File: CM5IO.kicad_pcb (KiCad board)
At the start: 4 copper layers, 65 parts, among them J10 690-019-298-412, J11 USB_C_Receptacle_USB2.0, J12 USB3_A, J14 JST_SHBM04B-SRSS-TB, J16 Conn_01x22_Female, J2 Conn_02x07_Odd_Even, J22 690-019-298-412, J3 Conn_01x03, J4 Bus_M.2_Socket_M, J5 Conn_01x22_Female, J6 THD-02-R, J8 THD-20-R, SW1 Right angle Tact button, U12 RT9742SNGV, U5 74LVC1G07SE-7, U6 AP22653W6, U7 ASEK-32.768KHZ-L-R-T, U8 AP3441SHE-7B

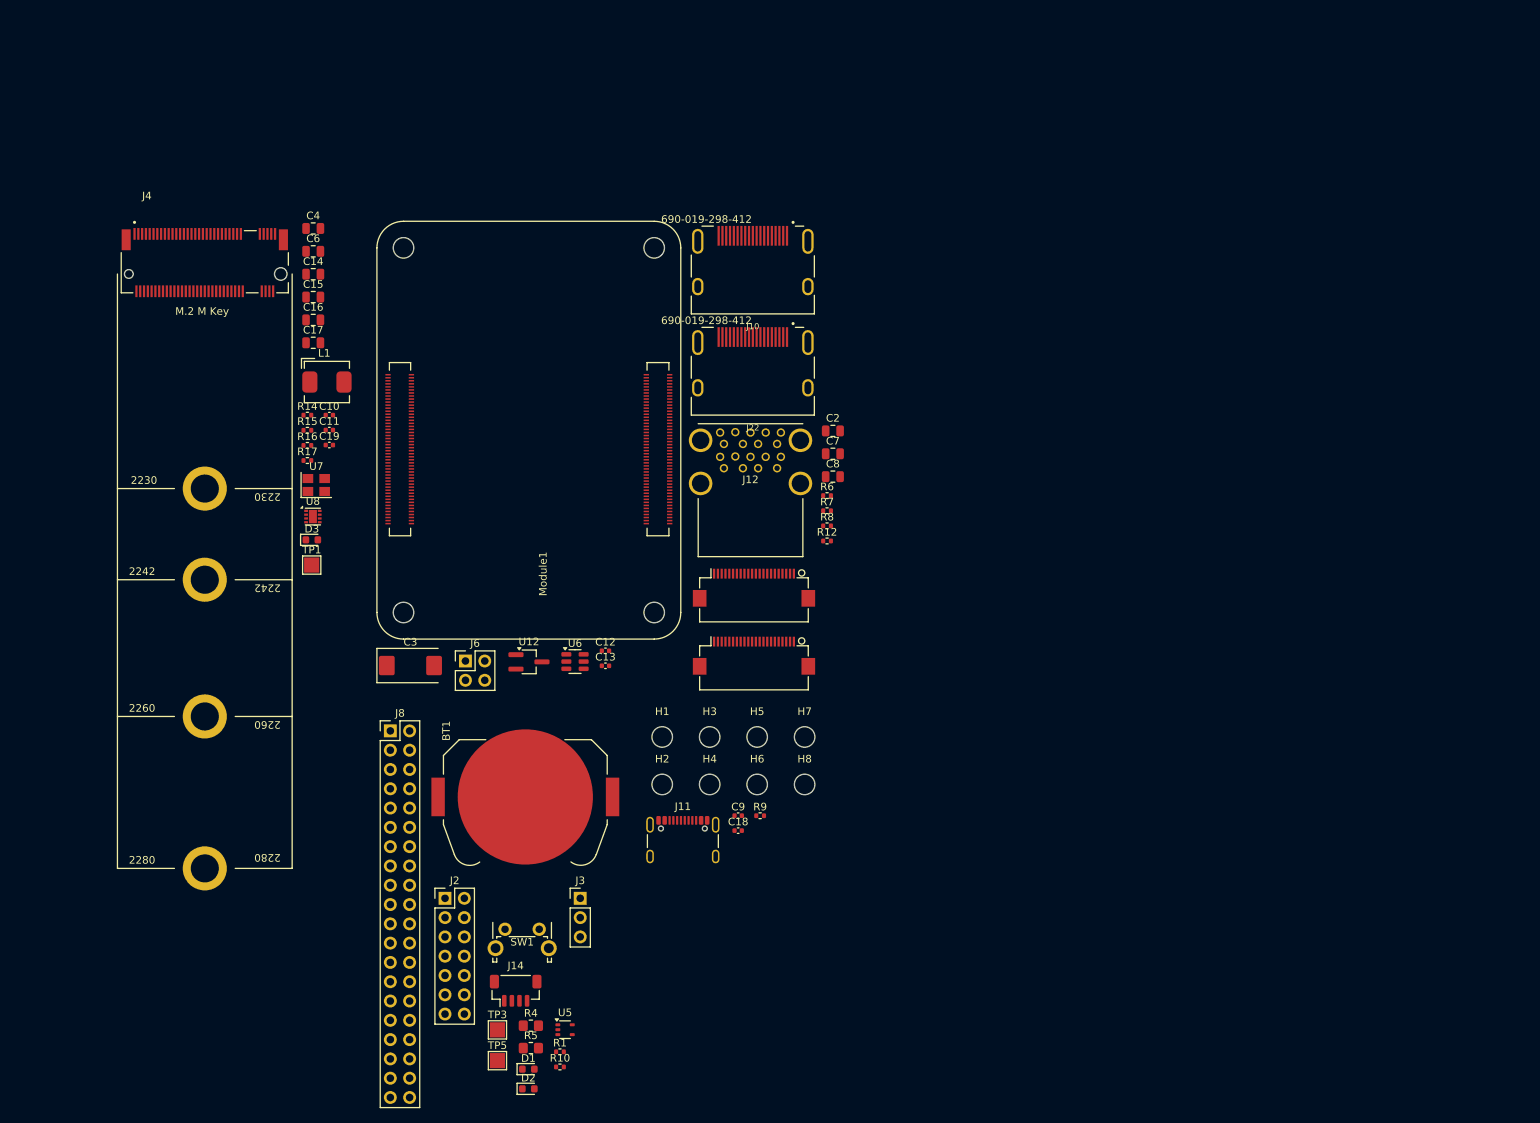
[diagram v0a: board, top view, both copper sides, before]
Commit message: Removing unwanted sections, such that the carrier board is a blank canvas
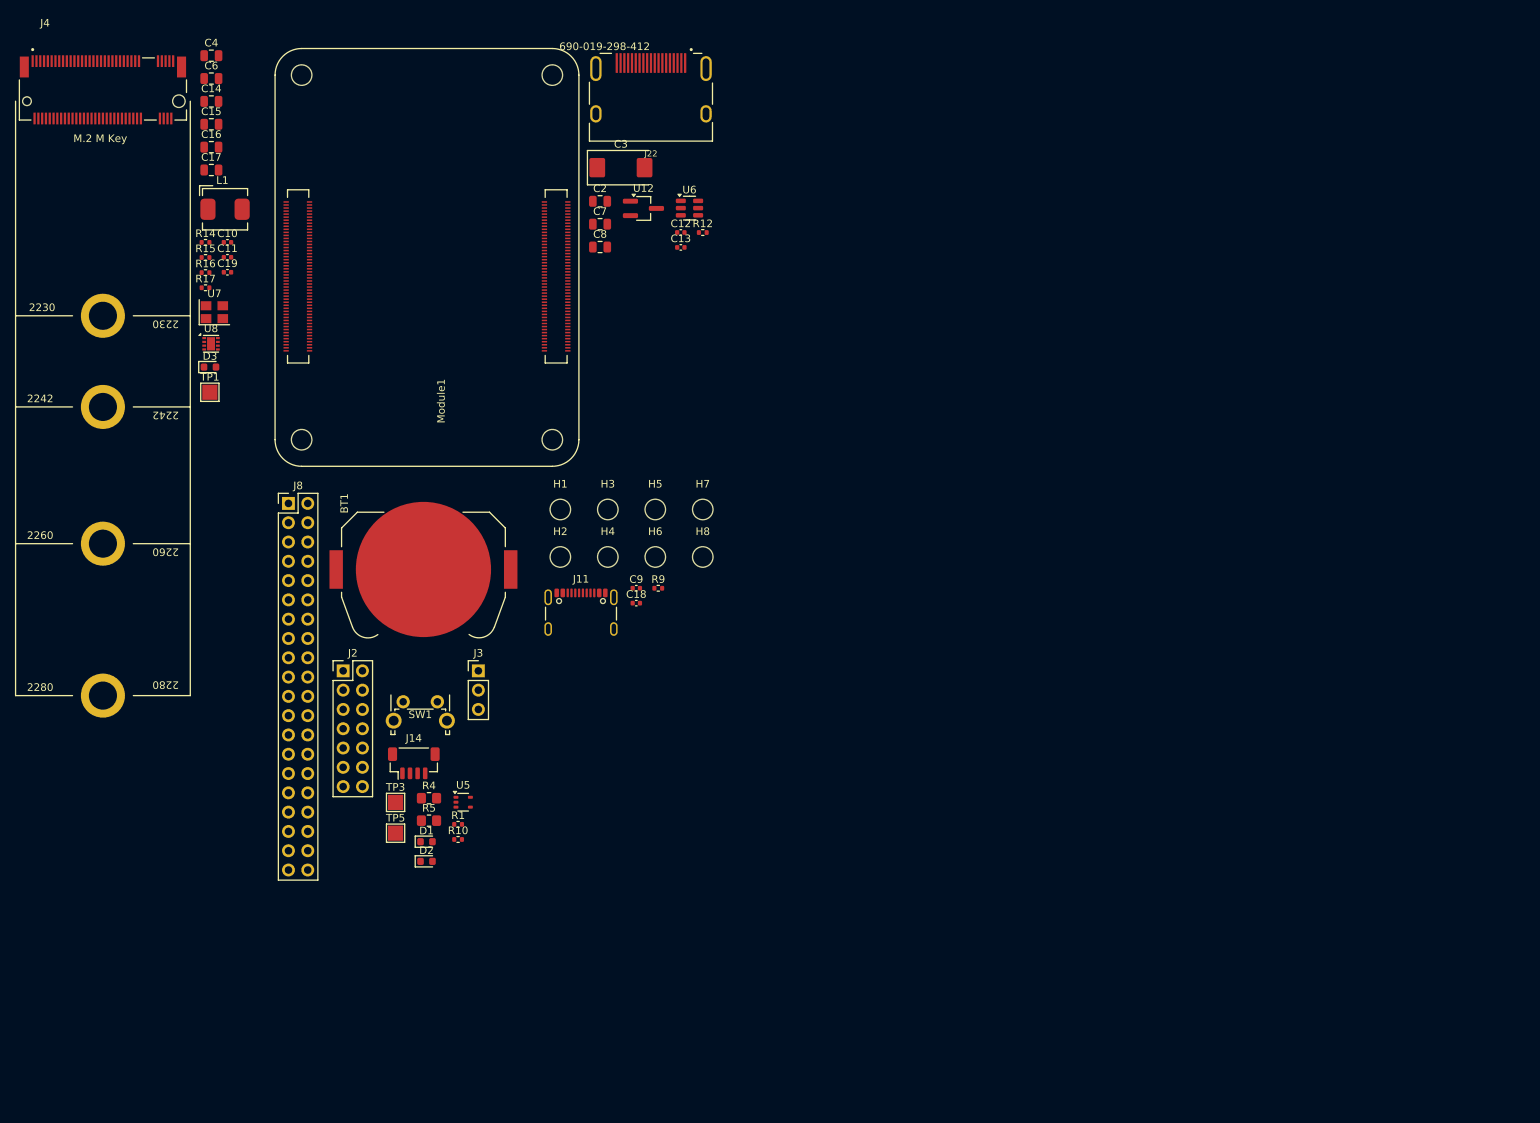
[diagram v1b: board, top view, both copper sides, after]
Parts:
- removed J10: 690-019-298-412, CM5IO:EDAC 690-019-298-412
- removed J12: USB3_A, CM5IO:MTCONN_UBAF30-D2011
- removed J16, J5: Conn_01x22_Female, CM5IO:Hirose_FH12-22S-0.5SH_1x22-1MP_P0.50mm_Horizontal
- removed J6: THD-02-R, Connector_PinHeader_2.54mm:PinHeader_2x02_P2.54mm_Vertical
- removed R6, R7, R8: 2.2K 1%, Resistor_SMD:R_0402_1005Metric
- moved C3 71.2 mm to (100.7, 41.9)
- moved U6 61.6 mm to (109.7, 47.2)
- moved U12 61.6 mm to (103.6, 47.2)
- moved C12 56.0 mm to (108.5, 50.4)
- moved C13 56.0 mm to (108.5, 52.4)
- moved R12 43.8 mm to (111.4, 50.4)
- moved C2 43.0 mm to (97.9, 46.3)
- moved C8 43.0 mm to (97.9, 52.3)
- moved C7 43.0 mm to (97.9, 49.3)
- moved J22 38.5 mm to (104.6, 28.8)
- moved R10 32.8 mm to (79.2, 130.3)
- moved J8 32.8 mm to (56.9, 86.1)
- moved BT1 32.8 mm to (74.7, 94.8)
- moved D1 32.8 mm to (75.1, 130.6)
- moved D2 32.8 mm to (75.1, 133.2)
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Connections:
- Module1 pad 80: /CM5_HighSpeed/SCL0 -> /CM5_GPIO ( Ethernet, GPIO, SDCARD)/SCL0
- Module1 pad 82: /CM5_HighSpeed/SDA0 -> /CM5_GPIO ( Ethernet, GPIO, SDCARD)/SDA0

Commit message: Added USB SS type A, thinking of replacing it in the future with USB type-c
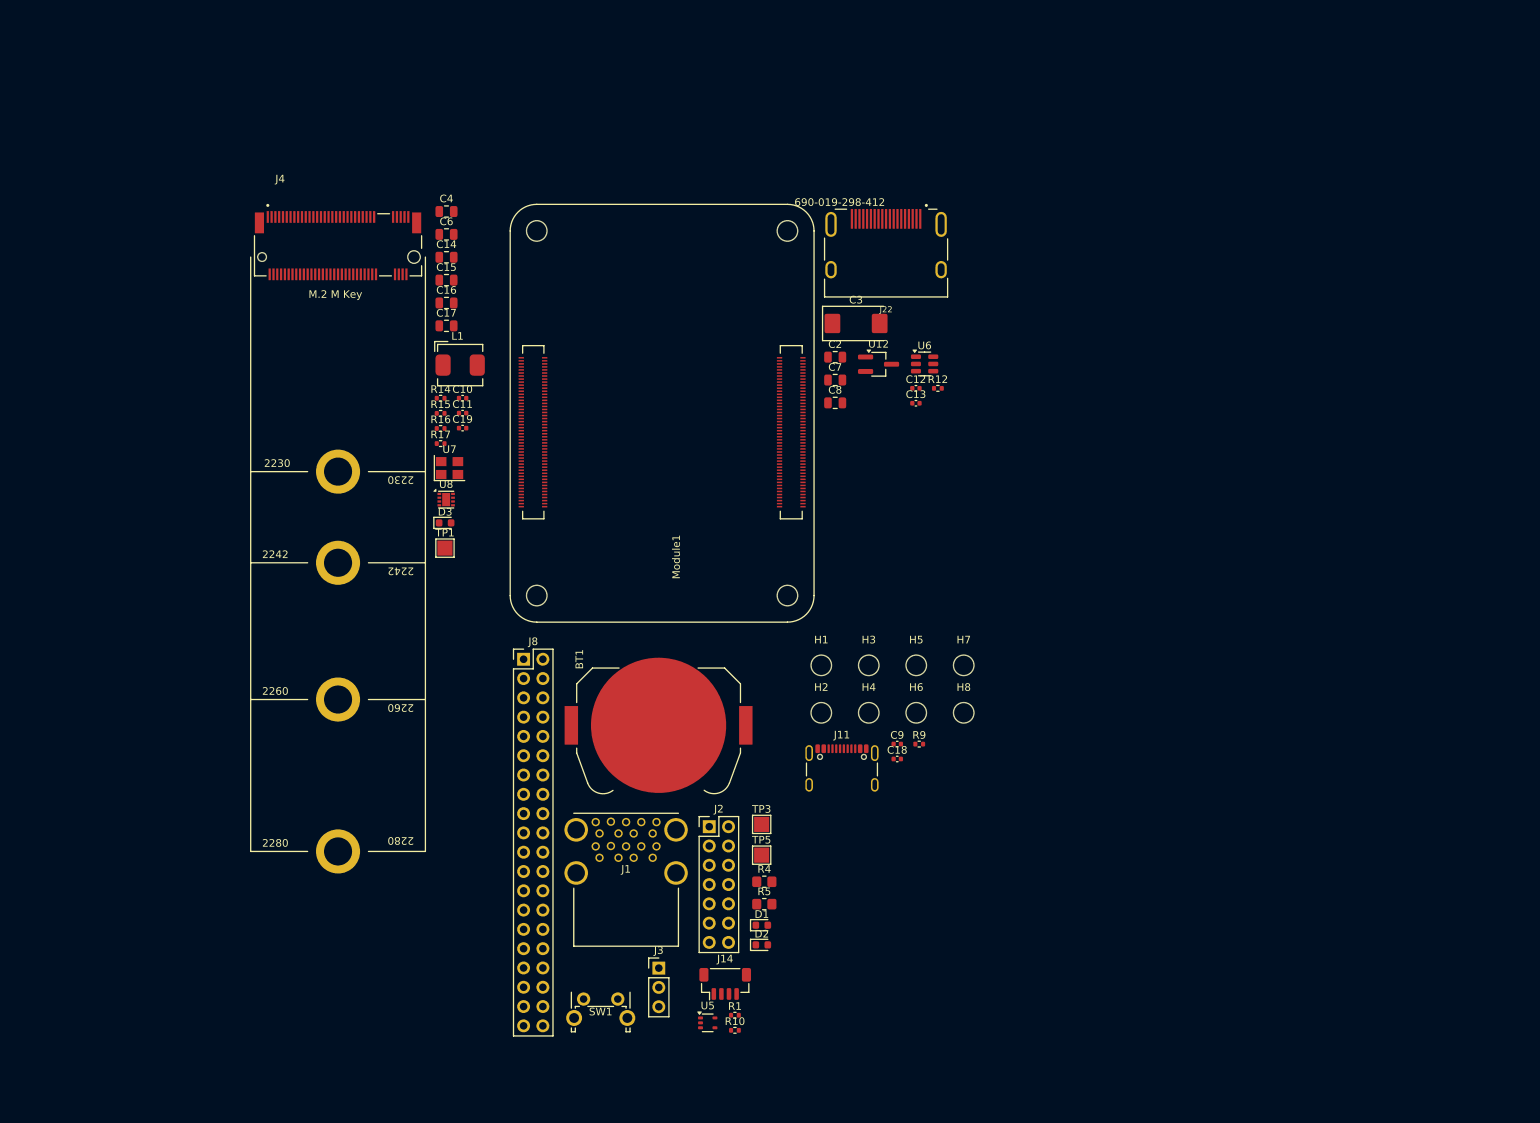
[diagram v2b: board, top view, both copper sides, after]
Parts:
- added J1: USB3_A, CM5IO:MTCONN_UBAF30-D2011, F.Cu at (101.3, 134.7)
- moved J2 52.4 mm to (112.3, 128.6)
- moved J14 50.2 mm to (114.4, 149.3)
- moved TP3 48.3 mm to (119.2, 128.3)
- moved TP5 48.3 mm to (119.2, 132.4)
- moved SW1 45.8 mm to (95.8, 151.3)
- moved J3 45.8 mm to (105.7, 147.3)
- moved D1 45.5 mm to (119.2, 141.6)
- moved D2 45.5 mm to (119.2, 144.2)
- moved R5 45.5 mm to (119.5, 138.8)
- moved R4 45.5 mm to (119.5, 135.9)
- moved R1 44.3 mm to (115.7, 153.5)
- moved R10 44.3 mm to (115.7, 155.4)
- moved U5 43.4 mm to (112.1, 154.5)
- moved H1 40.0 mm to (127.0, 107.4)
- moved H2 40.0 mm to (127.0, 113.7)
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
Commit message: Board development
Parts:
- removed H5, H6, H7, H8: MountingHole, CM5IO:MountingHole_2.7mm_M2.5_DIN965
- BT1, C10, C11, C14, C15, C16, C17, C2, C3, C4, C6, C7, C8, L1, R12, R14, R15, R16, U6, U8: moved to B.Cu
- moved TP1 137.8 mm to (215.0, 82.7), turned to 90 degrees
- moved D3 137.7 mm to (214.5, 74.2), turned to 180 degrees
- moved U7 137.6 mm to (215.0, 67.7), turned to 90 degrees
- moved R17 137.6 mm to (214.5, 79.2), turned to 180 degrees
- moved J4 137.1 mm to (200.5, 52.5)
- moved C19 134.7 mm to (214.5, 72.2)
- moved J2 131.1 mm to (215.7, 48.1)
- moved H2 114.3 mm to (217.5, 43.7)
- moved SW1 110.0 mm to (135.2, 48.7)
- moved BT1 107.7 mm to (202.5, 68.2), turned to 180 degrees
- moved R10 102.1 mm to (142.5, 57.0), turned to 180 degrees
- moved C4 100.1 mm to (176.6, 62.8), turned to 180 degrees
- moved C6 100.1 mm to (176.6, 65.8), turned to 180 degrees
- moved R1 98.0 mm to (134.0, 57.2)
- moved U5 97.6 mm to (139.6, 60.8)
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
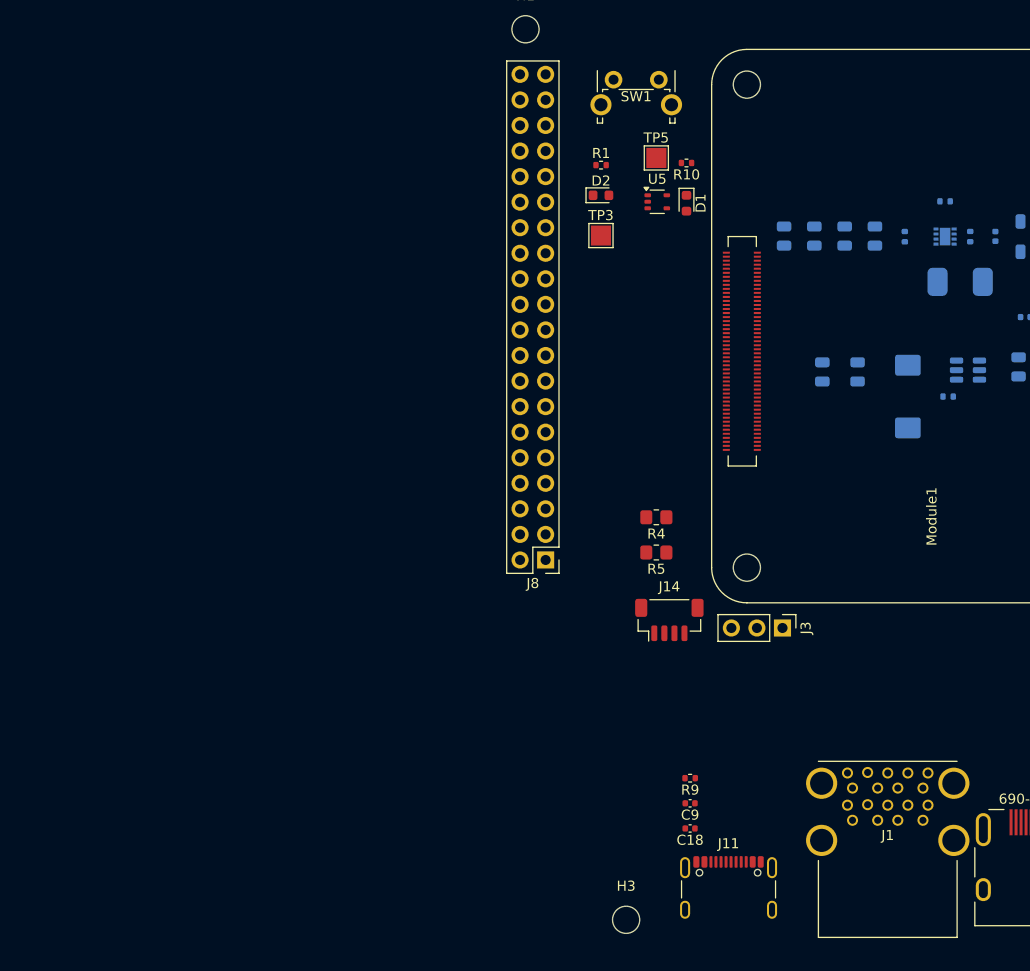
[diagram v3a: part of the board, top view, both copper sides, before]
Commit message: Included Cube pilot schematic symbol, pcb footprint and created another sheet.
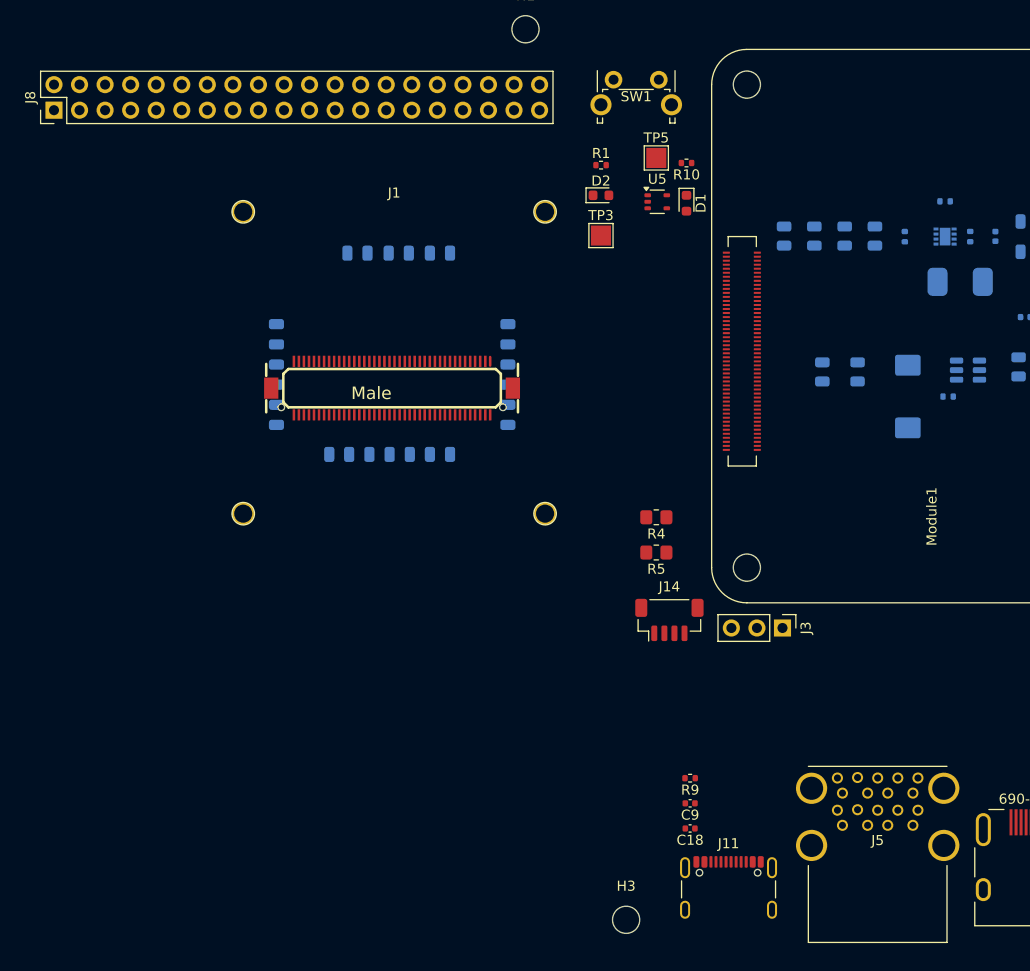
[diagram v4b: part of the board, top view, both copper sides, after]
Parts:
- added J5: USB3_A, CM5IO:MTCONN_UBAF30-D2011, F.Cu at (161.5, 124.8)
- added PSM1: Power Selection module, ALTIUM_Cube_footprint:PSM, B.Cu at (113.5, 75.7)
- J1: value USB3_A -> DF17_1.0H_-80DP-0.5V_57_; footprint CM5IO:MTCONN_UBAF30-D2011 -> ALTIUM_Cube_footprint:CON-DF17-80M
- moved J1 66.7 mm to (113.2, 79.4)
- moved J8 66.2 mm to (79.6, 51.7), turned to 90 degrees
